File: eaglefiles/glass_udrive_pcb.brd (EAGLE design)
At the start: 15.4 x 19.9 mm, 23 parts

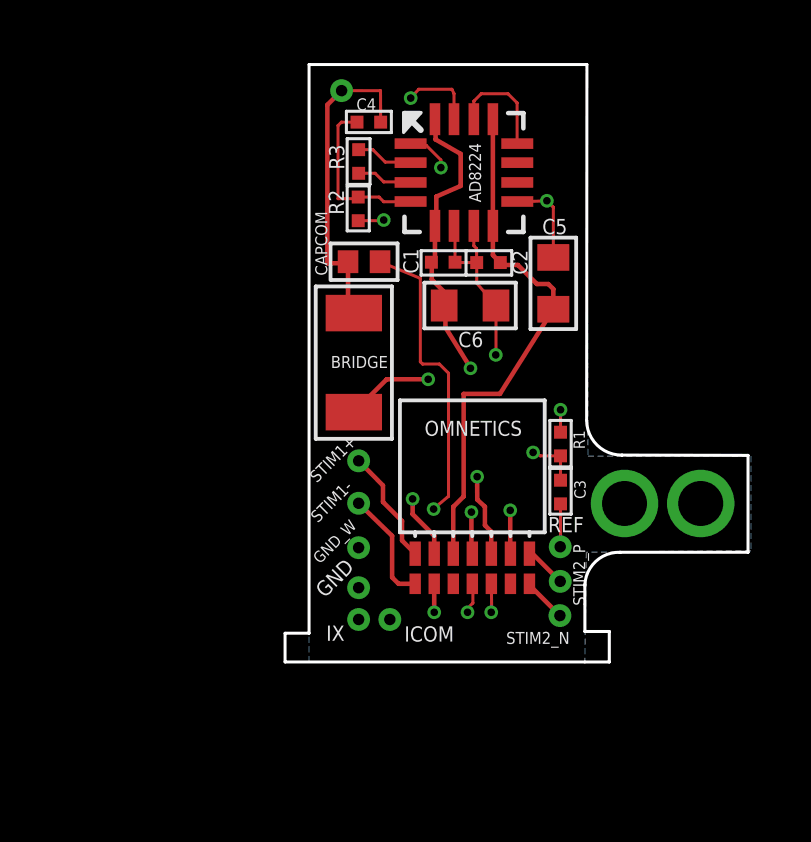
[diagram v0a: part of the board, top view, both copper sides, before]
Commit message: Dev branches merged into master branch. Optimizing the board routing and incorporating GFL comments: =========================== 1- top right of AD8224 (pins 12 and 13): don't run a trace under the corner of the chip, as per the data sheet. 2- power bypassing: capacitor placement does not agree with datasheet recommendation (pg 23 § "Power supplies" ¶ 3 sentence 2) 3- via placement for bypass capacitors should be as close as possible to the 0.1uF caps 4- power planes: you could easily use copper pours instead of traces for the copper planes here, I think you could move the few traces on the internal layers around a pour. 5- gain resistor should be as close to pin 2 and 3 as possible, with equal capacitances. I think they could stand to be closer. Maybe rotating the AD8224 90 degrees clockwise would allow for tighter routing of high-impendace low voltage signals, minimizing the chance of noise sources coupling into the system. Be wary during construction of the +-15V hoving right over the elctrode traces. As the wires move w.r.t. the high impedance traces, the capacitance will vary with the motion inducing current flow (and therefore voltage). 6- C6 may block the connector. I would see how much clearance you have and if the bend angle you're hoping for is achievable. (you can look at my boards as an example of what bend angle is possible) ============================
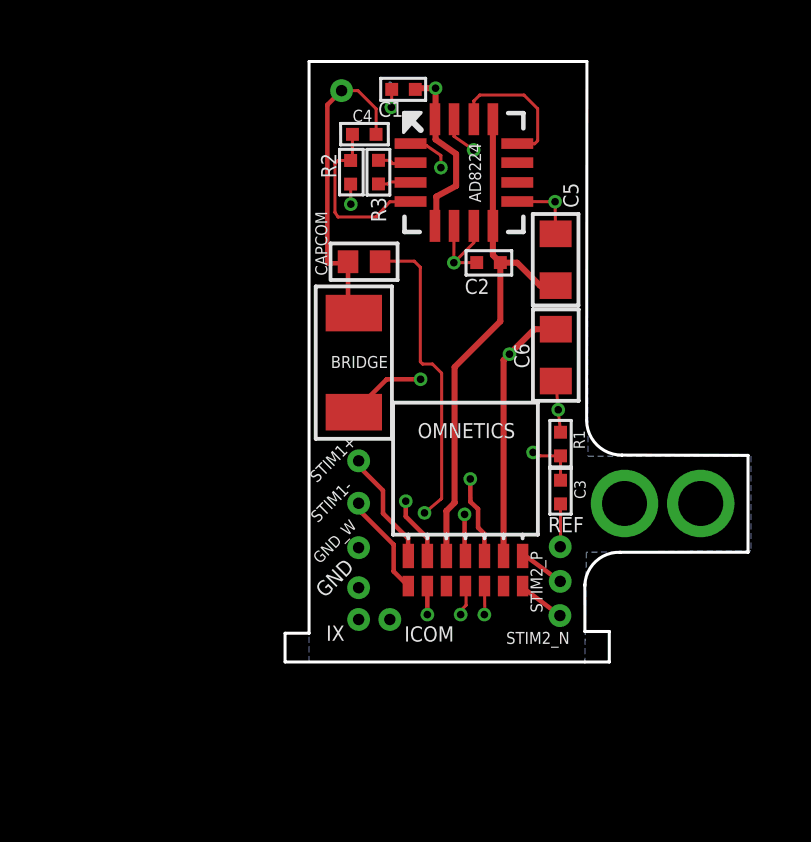
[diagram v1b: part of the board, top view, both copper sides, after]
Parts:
- moved C1 5.91 mm to (2.39, 18.7), turned to 0 degrees
- moved C6 3.30 mm to (7.46, 9.82), turned to 90 degrees
- moved R2 1.25 mm to (0.62, 15.9)
- moved C5 0.79 mm to (7.46, 13.0)
- moved R3 0.75 mm to (1.55, 15.9)
- moved C4 0.43 mm to (1.08, 17.2)
- moved OMNETICS 0.24 mm to (4.45, 2.59)
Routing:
- net +15V: track 16.8 -> 25.9 mm
- net GND: track 13.0 -> 10.9 mm, vias 7 -> 8
- net CHAN2_OUT: track 3.63 -> 4.81 mm
- net GLASS_OUT: track 21.7 -> 20.8 mm
- net I_COM: track 10.4 -> 9.54 mm
- net N$2: track 1.91 -> 1.13 mm
- net N$4: track 1.86 -> 1.11 mm
- net BRG_BAL: track 12.7 -> 13.3 mm
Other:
- board size 15.4 x 19.9 mm -> 15.4 x 20 mm

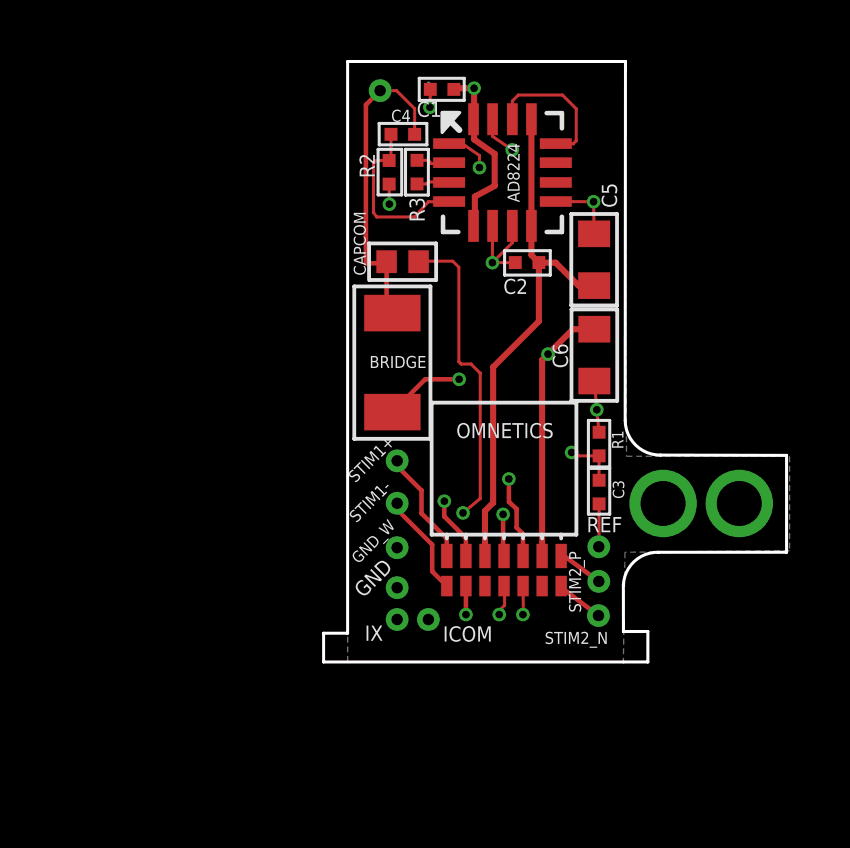
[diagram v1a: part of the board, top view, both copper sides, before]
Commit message: updated several board layout details: made it smaller H and W, changed the anchoring tab on the opposite side, added +-15 power supply pours to simplify routing and reduced bridge resistor size to 408 package 1/16 W 100Mohm resistor.
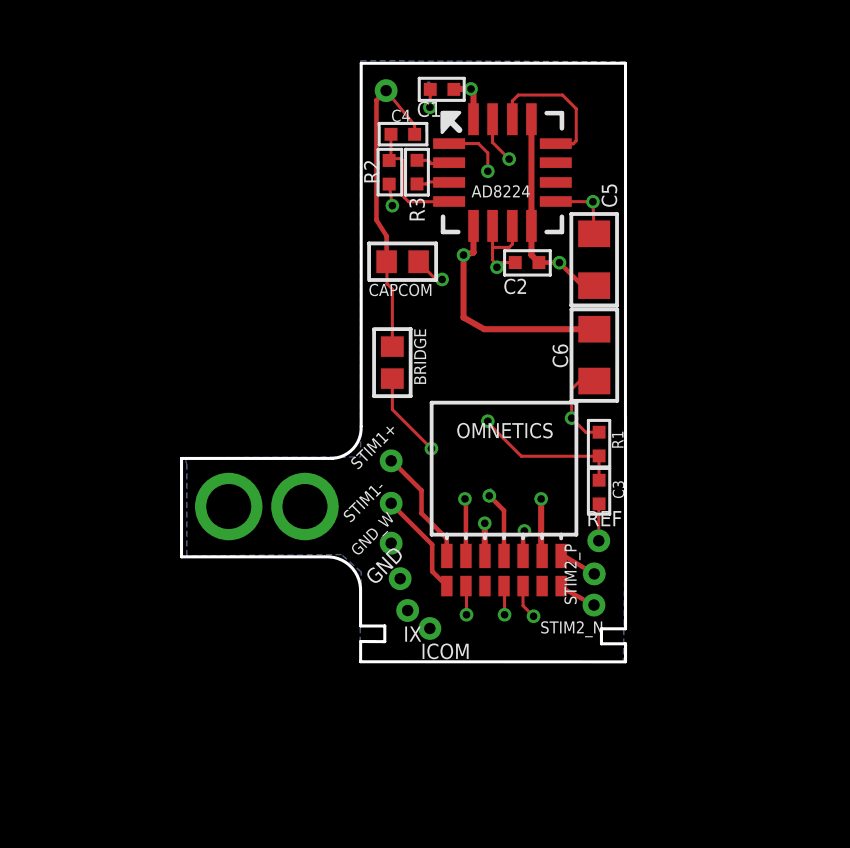
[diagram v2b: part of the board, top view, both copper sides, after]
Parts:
- BRIDGE: device GFL:1206 -> GFL:0402
- moved IX 0.46 mm to (1.24, 1.31)
- moved STIM2_N 0.38 mm to (7.45, 1.49)
- moved GND 0.32 mm to (0.99, 2.37)
- moved ICOM 0.30 mm to (1.98, 0.71)
- moved STIM2_P 0.29 mm to (7.46, 2.53)
- moved GND_W 0.25 mm to (0.69, 3.55)
- moved STIM1+ 0.20 mm to (0.69, 6.30)
- moved STIM1- 0.20 mm to (0.69, 4.88)
- moved GLASS 0.20 mm to (0.52, 18.6)
- moved REF 0.20 mm to (7.61, 3.63)
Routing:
- net +15V: track 25.9 -> 20.6 mm, vias 2 -> 3
- net I_COM: track 9.54 -> 6.18 mm
- net GLASS_OUT: track 20.8 -> 17.8 mm
- net -15V: track 17.6 -> 19.9 mm, vias 0 -> 2
- net GND: track 10.9 -> 13.1 mm
- net GLASS_FLT: track 5.92 -> 4.12 mm
- net REF_FLT: track 14.2 -> 15.6 mm
- net CAP_COM: track 14.9 -> 13.8 mm
- net BRG_BAL: track 13.3 -> 13.9 mm
- added copper zone on layer 2, net +15V
- added copper zone on layer 2, net -15V
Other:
- board size 15.4 x 20 mm -> 14.8 x 20 mm
- board text removed: "Head-plate mounting"

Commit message: Move bridge balance resistor up and trace from glass electrode to CAPCOM to layer 15
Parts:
- moved BRIDGE 1.45 mm to (0.73, 11.0)
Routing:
- net BRG_BAL: track 13.9 -> 15.3 mm
- net GLASS: track 10.6 -> 9.54 mm, vias 0 -> 1
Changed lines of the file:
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@@
 <setting verticaltext="up"/>
 </settings>
-<grid distance="1.96850394" unitdist="mil" unit="mil" style="lines" multiple="1" display="yes" altdistance="0.001" altunitdist="mm" altunit="mm"/>
+<grid distance="1.96850394" unitdist="mil" unit="mil" style="lines" multiple="1" display="no" altdistance="0.001" altunitdist="mm" altunit="mm"/>
 <layers>
 <layer number="1" name="Top" color="4" fill="1" visible="yes" active="yes"/>
-<layer number="2" name="Route2" color="57" fill="1" visible="yes" active="yes"/>
+<layer number="2" name="Route2" color="13" fill="4" visible="yes" active="yes"/>
 <layer number="3" name="Route3" color="4" fill="3" visible="no" active="no"/>
 <layer number="14" name="Route14" color="1" fill="6" visible="no" active="no"/>
-<layer number="15" name="Route15" color="24" fill="1" visible="yes" active="yes"/>
+<layer number="15" name="Route15" color="11" fill="5" visible="yes" active="yes"/>
 <layer number="16" name="Bottom" color="1" fill="1" visible="yes" active="yes"/>
 <layer number="17" name="Pads" color="2" fill="1" visible="yes" active="yes"/>
@@
 </element>
 <element name="CAPCOM" library="GFL" package="0402" value="10pF" x="1.07050625" y="12.9356" smashed="yes">
-<attribute name="NAME" x="2.07769375" y="12.1944" size="0.4" layer="25" font="vector" ratio="12" rot="R180"/>
+<attribute name="NAME" x="2.3556" y="13.62769375" size="0.4" layer="25" font="vector" ratio="12" rot="R270"/>
 <attribute name="VALUE" x="-0.19949375" y="11.1576" size="0.762" layer="27" font="vector" ratio="12"/>
 </element>
@@
 <attribute name="NAME" x="6.1092" y="7.5558" size="0.5" layer="25" font="vector" ratio="12" rot="R180"/>
 </element>
-<element name="BRIDGE" library="GFL" package="0402" value="100MOhm" x="0.729678125" y="9.57209375" smashed="yes" rot="R270">
-<attribute name="NAME" x="1.456478125" y="10.71569375" size="0.4" layer="25" font="vector" ratio="12" rot="R270"/>
-<attribute name="VALUE" x="-1.048321875" y="10.84209375" size="0.762" layer="27" font="vector" ratio="12" rot="R270"/>
+<element name="BRIDGE" library="GFL" package="0402" value="100MOhm" x="0.729678125" y="11.02209375" smashed="yes" rot="R270">
+<attribute name="NAME" x="0.08430625" y="9.406478125" size="0.4" layer="25" font="vector" ratio="12"/>
+<attribute name="VALUE" x="-1.048321875" y="12.29209375" size="0.762" layer="27" font="vector" ratio="12" rot="R270"/>
 </element>
 <element name="STIM1-" library="GFL" package="30MIL/15MIL" value="" x="0.69" y="4.884" smashed="yes">
@@
 <via x="2.032" y="6.7056" extent="1-16" drill="0.254"/>
 <wire x1="2.032" y1="6.7056" x2="2.032" y2="7.0104" width="0.1016" layer="1"/>
-<wire x1="0.729678125" y1="9.03869375" x2="0.729678125" y2="8.007921875" width="0.1016" layer="1"/>
+<wire x1="0.729678125" y1="10.48869375" x2="0.729678125" y2="8.007921875" width="0.1016" layer="1"/>
 <wire x1="0.729678125" y1="8.007921875" x2="2.032" y2="6.7056" width="0.1016" layer="1"/>
 </signal>
@@
 <wire x1="1.4713" y1="17.4893" x2="0.5222" y2="18.6384" width="0.1016" layer="1"/>
 <wire x1="0.53710625" y1="12.9356" x2="0.53710625" y2="13.78849375" width="0.1524" layer="1"/>
-<wire x1="0.53710625" y1="13.78849375" x2="0.2" y2="14.3256" width="0.1524" layer="1"/>
-<wire x1="0.2" y1="14.3256" x2="0.2" y2="18.3162" width="0.1524" layer="1"/>
-<wire x1="0.2" y1="18.3162" x2="0.5222" y2="18.6384" width="0.1524" layer="1"/>
-<wire x1="0.729678125" y1="10.10549375" x2="0.729678125" y2="12.020321875" width="0.1016" layer="1"/>
+<wire x1="0.53710625" y1="13.78849375" x2="1.2" y2="14.3256" width="0.1524" layer="15"/>
+<wire x1="1.2" y1="14.3256" x2="1.15" y2="18.0162" width="0.1524" layer="15"/>
+<wire x1="1.15" y1="18.0162" x2="0.5222" y2="18.6384" width="0.1524" layer="15"/>
+<wire x1="0.729678125" y1="11.55549375" x2="0.729678125" y2="12.020321875" width="0.1016" layer="1"/>
 <wire x1="0.729678125" y1="12.020321875" x2="0.55" y2="12.2" width="0.1016" layer="1"/>
 <wire x1="0.55" y1="12.2" x2="0.55" y2="12.92270625" width="0.1016" layer="1"/>
 <wire x1="0.55" y1="12.92270625" x2="0.53710625" y2="12.9356" width="0.1016" layer="1"/>
+<via x="0.53710625" y="13.78849375" extent="1-16" drill="0.254"/>
 </signal>
 <signal name="GLASS_OUT">

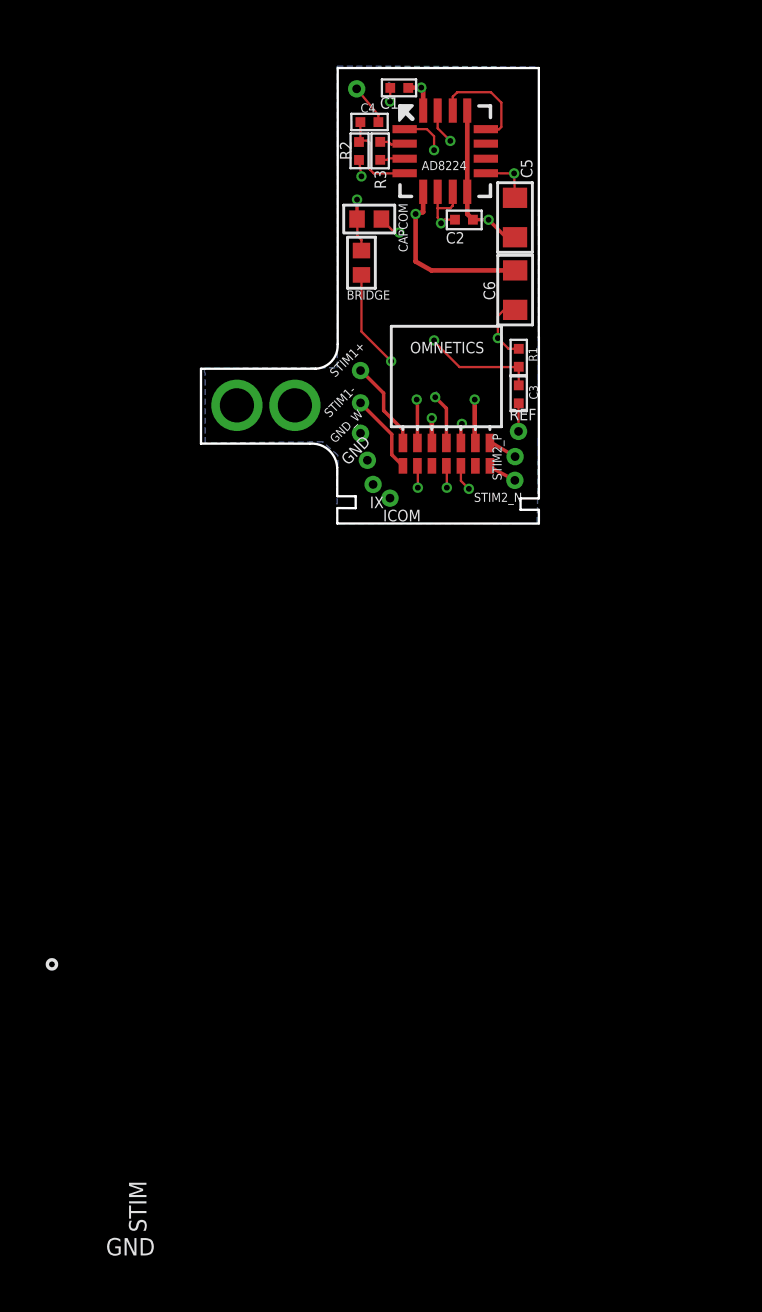
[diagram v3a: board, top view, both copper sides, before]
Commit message: Added optional circuit for 2nd INA channel and routing optimized.
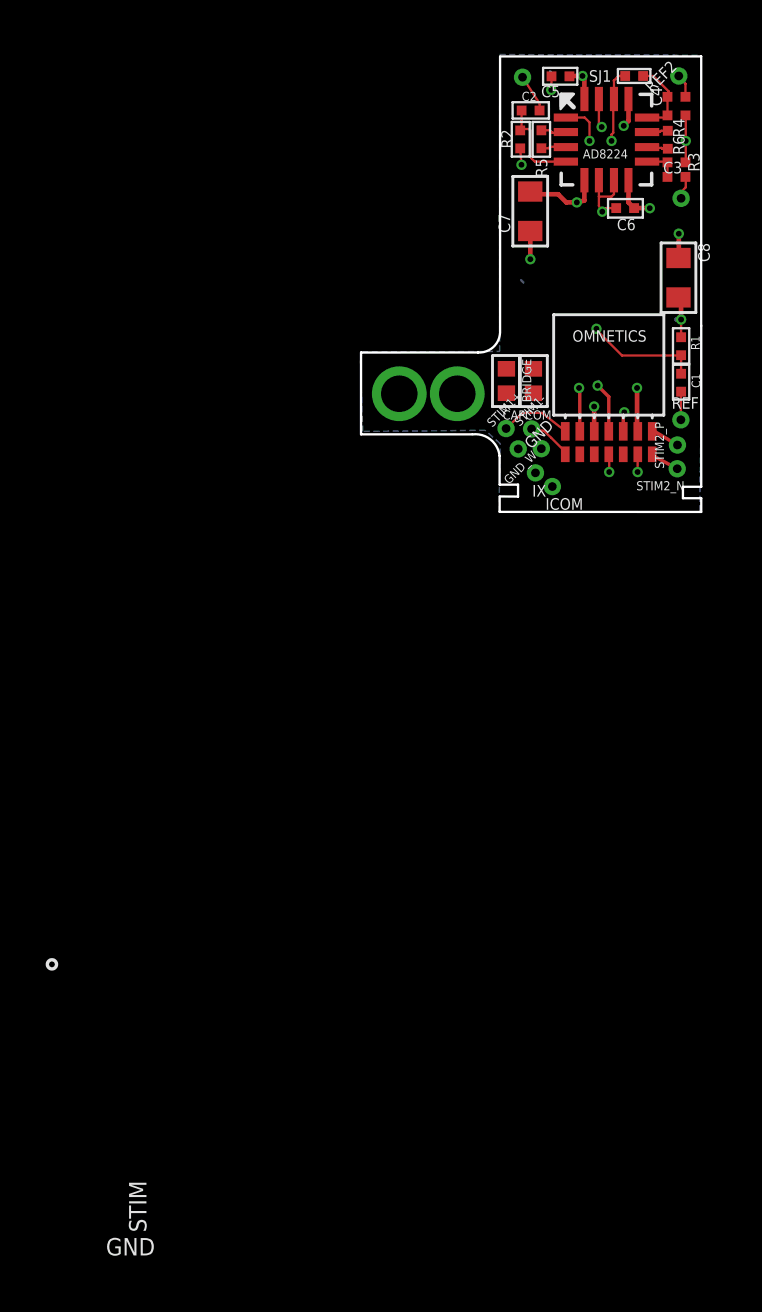
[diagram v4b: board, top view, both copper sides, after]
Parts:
- added C7, C8: 10uF, GFL:0603
- added R4: 10Mohm, GFL:0201
- added R5, R6: 5.49KOhm, GFL:0201
- added REF2, SIG2: (no value), GFL:30MIL/15MIL
- added SJ1: (no value), GFL:0201
- C1, C2: value 0.1uF -> 6800pF
- C5, C6: value 10uF -> 0.1uF; device GFL:0603 -> GFL:0201
- R3: value 5.49KOhm -> 10Mohm
- moved C1 17.9 mm to (14.7, 5.77), turned to 90 degrees
- moved C4 13.5 mm to (14.5, 18.3)
- moved R3 13.0 mm to (14.5, 15.4), turned to 180 degrees
- moved C3 11.8 mm to (14.5, 14.8), turned to 180 degrees
- moved CAPCOM 10.1 mm to (8.26, 5.84), turned to 270 degrees
- moved BRIDGE 8.20 mm to (7.08, 5.84)
- moved GND 7.64 mm to (8.61, 2.88)
- moved STIM1- 7.58 mm to (8.18, 3.74)
- moved GLASS 7.28 mm to (7.79, 19.1)
- moved ICOM 7.13 mm to (9.09, 1.22)
- moved IX 7.13 mm to (8.35, 1.82)
- moved OMNETICS 7.13 mm to (11.6, 3.10)
- moved R1 7.13 mm to (14.7, 7.37)
- moved REF 7.13 mm to (14.7, 4.14)
- moved STIM2_N 7.13 mm to (14.6, 2.00)
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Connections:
- removed net METAL_OUT: OMNETICS.D
- new net N$6: AD8224.10, R6.2
- new net N$7: AD8224.11, R6.1
- new net REF2: C4.1, REF2.P$1
- new net REF_FLT2: AD8224.12, C4.2, R4.2, SJ1.2
- new net SIG2: C3.1, SIG2.P$1
- new net SIG2_FLT: AD8224.9, C3.2, R3.2
- net +15V: now also C5.2, C7.2; no longer C1.2, C6.2
- net -15V: now also C6.2, C8.2; no longer C2.2, C5.2
- net CHAN2_OUT: now also OMNETICS.D, SJ1.1; no longer AD8224.12
- net GLASS: now also C2.1; no longer C4.1
- net GLASS_FLT: now also C2.2; no longer C4.2
- net GND: now also C7.1, C8.1, R3.1, R4.1; no longer AD8224.9, C1.1, C2.1
- net N$2: now also R5.2; no longer R3.2
- net N$4: now also R5.1; no longer R3.1
- net REF: now also C1.1; no longer C3.1
- net REF_FLT: now also C1.2; no longer C3.2
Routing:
- net BRG_BAL: track 15.3 -> 0.00 mm, vias 2 -> 0
- net CHAN2_OUT: track 4.81 -> 19.4 mm, vias 0 -> 2
- net CAP_COM: track 13.8 -> 0.00 mm, vias 2 -> 0
- net GLASS: track 9.54 -> 1.68 mm, vias 1 -> 0
- net +15V: track 20.6 -> 16.4 mm
- net REF_FLT2: track 0.00 -> 3.41 mm
- net SIG2_FLT: track 0.00 -> 1.60 mm
- net STIM1_N: track 3.53 -> 1.96 mm
- net -15V: track 19.9 -> 18.7 mm, vias 2 -> 4
- net SIG2: track 0.00 -> 1.15 mm
- net REF2: track 0.00 -> 1.02 mm
- net N$6: track 0.00 -> 0.94 mm
- net N$7: track 0.00 -> 0.93 mm
- net STIM1_P: track 3.95 -> 3.16 mm
- net GND: track 13.1 -> 13.4 mm, vias 8 -> 9
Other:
- board size 14.8 x 20 mm -> 14.9 x 20 mm
